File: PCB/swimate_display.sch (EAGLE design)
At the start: 53 parts, among them IC1 LPC11U24, T1 BSS84, T2 BSS84, U1 USD-SOCKETNEW, U5 DS3231MZ/V+T, U6 MAX1595EUA33+, U7 MAX1811ESA-T, U8 MAX16054AZT+T, U9 HC_05, Y1 12.000MHz

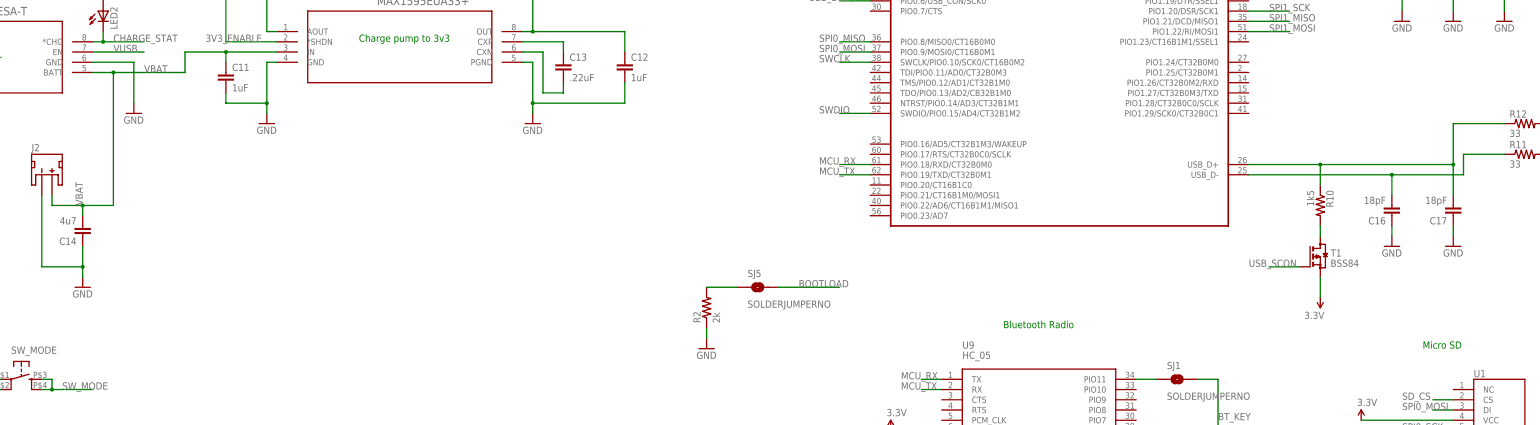
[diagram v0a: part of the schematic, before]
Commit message: changed pcb size and separated display portion
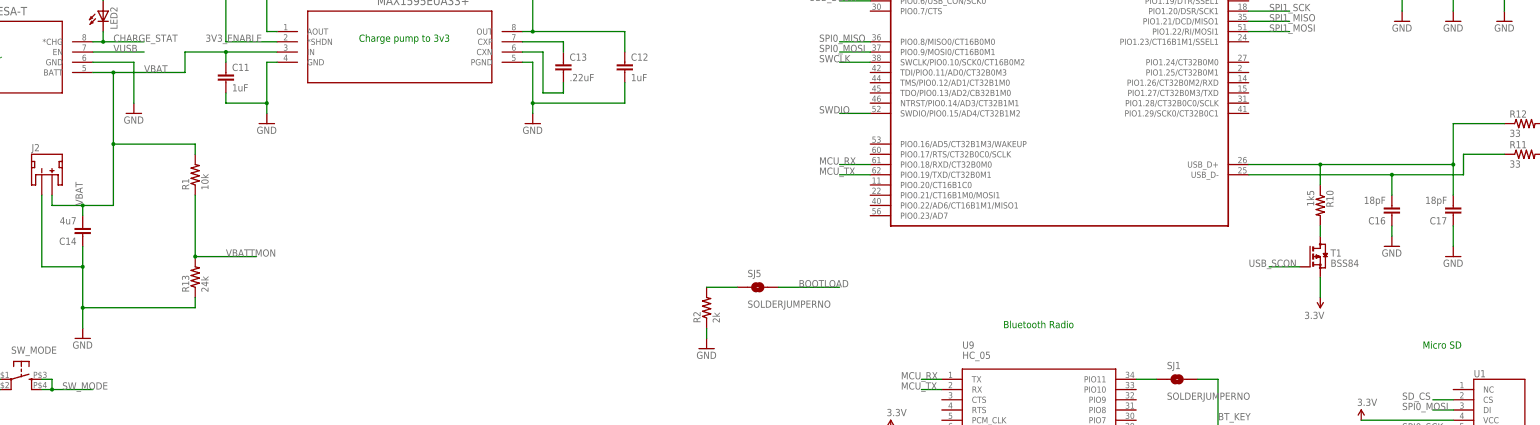
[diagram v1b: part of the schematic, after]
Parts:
- added R1: 10k, SparkFun-Passives:RESISTOR0603-RES
- added R13: 24k, SparkFun-Passives:RESISTOR0603-RES
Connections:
- new net VBATTMON: R1.1, R13.2
- net GND: now also R13.1
- net VBAT: now also R1.2
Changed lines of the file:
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@@
 <?xml version="1.0" encoding="utf-8"?>
 <!DOCTYPE eagle SYSTEM "eagle.dtd">
-<eagle version="6.5.0">
+<eagle version="6.4">
 <drawing>
 <settings>
@@
 <part name="SW_MODE" library="SparkFun-Electromechanical" deviceset="TAC_SWITCH" device="KSA_SEALED"/>
 <part name="GND32" library="SparkFun-Aesthetics" deviceset="GND" device=""/>
+<part name="R1" library="SparkFun-Passives" deviceset="RESISTOR" device="0603-RES" value="10k"/>
+<part name="R13" library="SparkFun-Passives" deviceset="RESISTOR" device="0603-RES" value="24k"/>
 </parts>
 <sheets>
@@
 <instance part="C14" gate="G$1" x="-233.68" y="2.54" rot="R180"/>
 <instance part="J2" gate="G$1" x="-243.84" y="15.24"/>
-<instance part="GND20" gate="1" x="-233.68" y="-12.7"/>
+<instance part="GND20" gate="1" x="-233.68" y="-25.4"/>
 <instance part="JP3" gate="G$1" x="149.86" y="20.32"/>
 <instance part="GND21" gate="1" x="-294.64" y="33.02"/>
@@
 <instance part="R12" gate="G$1" x="124.46" y="27.94"/>
 <instance part="SUPPLY10" gate="G$1" x="73.66" y="-15.24" rot="R180"/>
-<instance part="GND27" gate="1" x="106.68" y="-2.54"/>
+<instance part="GND27" gate="1" x="106.68" y="-5.08"/>
 <instance part="GND28" gate="1" x="91.44" y="-2.54"/>
 <instance part="C16" gate="G$1" x="91.44" y="7.62" rot="R180"/>
@@
 <instance part="SW_MODE" gate="S" x="-248.92" y="-35.56"/>
 <instance part="GND32" gate="1" x="-261.62" y="-48.26"/>
+<instance part="R1" gate="G$1" x="-205.74" y="15.24" rot="R90"/>
+<instance part="R13" gate="G$1" x="-205.74" y="-10.16" rot="R90"/>
 </instances>
 <busses>
@@
 <pinref part="U7" gate="A" pin="BATT"/>
 <wire x1="-231.14" y1="40.64" x2="-226.06" y2="40.64" width="0.1524" layer="91"/>
-<wire x1="-226.06" y1="40.64" x2="-226.06" y2="7.62" width="0.1524" layer="91"/>
+<wire x1="-226.06" y1="40.64" x2="-226.06" y2="22.86" width="0.1524" layer="91"/>
+<wire x1="-226.06" y1="22.86" x2="-226.06" y2="7.62" width="0.1524" layer="91"/>
 <wire x1="-226.06" y1="7.62" x2="-233.68" y2="7.62" width="0.1524" layer="91"/>
 <junction x="-233.68" y="7.62"/>
@@
 <junction x="-198.12" y="45.72"/>
 <label x="-218.44" y="40.64" size="1.778" layer="95"/>
+<pinref part="R1" gate="G$1" pin="2"/>
+<wire x1="-205.74" y1="20.32" x2="-205.74" y2="22.86" width="0.1524" layer="91"/>
+<wire x1="-205.74" y1="22.86" x2="-226.06" y2="22.86" width="0.1524" layer="91"/>
+<junction x="-226.06" y="22.86"/>
 </segment>
 </net>
@@
 <wire x1="-243.84" y1="-7.62" x2="-233.68" y2="-7.62" width="0.1524" layer="91"/>
 <pinref part="C14" gate="G$1" pin="1"/>
-<wire x1="-233.68" y1="-7.62" x2="-233.68" y2="-10.16" width="0.1524" layer="91"/>
+<wire x1="-233.68" y1="-7.62" x2="-233.68" y2="-17.78" width="0.1524" layer="91"/>
+<wire x1="-233.68" y1="-17.78" x2="-233.68" y2="-22.86" width="0.1524" layer="91"/>
 <wire x1="-233.68" y1="-2.54" x2="-233.68" y2="-7.62" width="0.1524" layer="91"/>
 <junction x="-233.68" y="-7.62"/>
+<pinref part="R13" gate="G$1" pin="1"/>
+<wire x1="-205.74" y1="-15.24" x2="-205.74" y2="-17.78" width="0.1524" layer="91"/>
+<wire x1="-205.74" y1="-17.78" x2="-233.68" y2="-17.78" width="0.1524" layer="91"/>
+<junction x="-233.68" y="-17.78"/>
 </segment>
 <segment>
@@
 <pinref part="C17" gate="G$1" pin="1"/>
 <pinref part="GND27" gate="1" pin="GND"/>
-<wire x1="106.68" y1="2.54" x2="106.68" y2="0" width="0.1524" layer="91"/>
+<wire x1="106.68" y1="2.54" x2="106.68" y2="-2.54" width="0.1524" layer="91"/>
 </segment>
 <segment>
@@
 </segment>
 </net>
+<net name="VBATTMON" class="0">
+<segment>
+<pinref part="R13" gate="G$1" pin="2"/>
+<wire x1="-205.74" y1="-5.08" x2="-190.5" y2="-5.08" width="0.1524" layer="91"/>
+<junction x="-205.74" y="-5.08"/>
+<label x="-198.12" y="-5.08" size="1.778" layer="95"/>
+<pinref part="R1" gate="G$1" pin="1"/>
+<wire x1="-205.74" y1="10.16" x2="-205.74" y2="-5.08" width="0.1524" layer="91"/>
+</segment>
+</net>
